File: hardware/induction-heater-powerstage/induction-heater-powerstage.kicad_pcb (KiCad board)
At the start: 2 copper layers, 112.8 x 55 mm, 17 parts, among them IC1 MAX17601ASA+, J2 Screw_Terminal_01x02, J3 Screw_Terminal_01x01, J4 Screw_Terminal_01x01, J5 Screw_Terminal_01x01, J6 Screw_Terminal_01x01, J7 RJ12, Q1 NTH4L040N120M3S, Q3 NTH4L040N120M3S

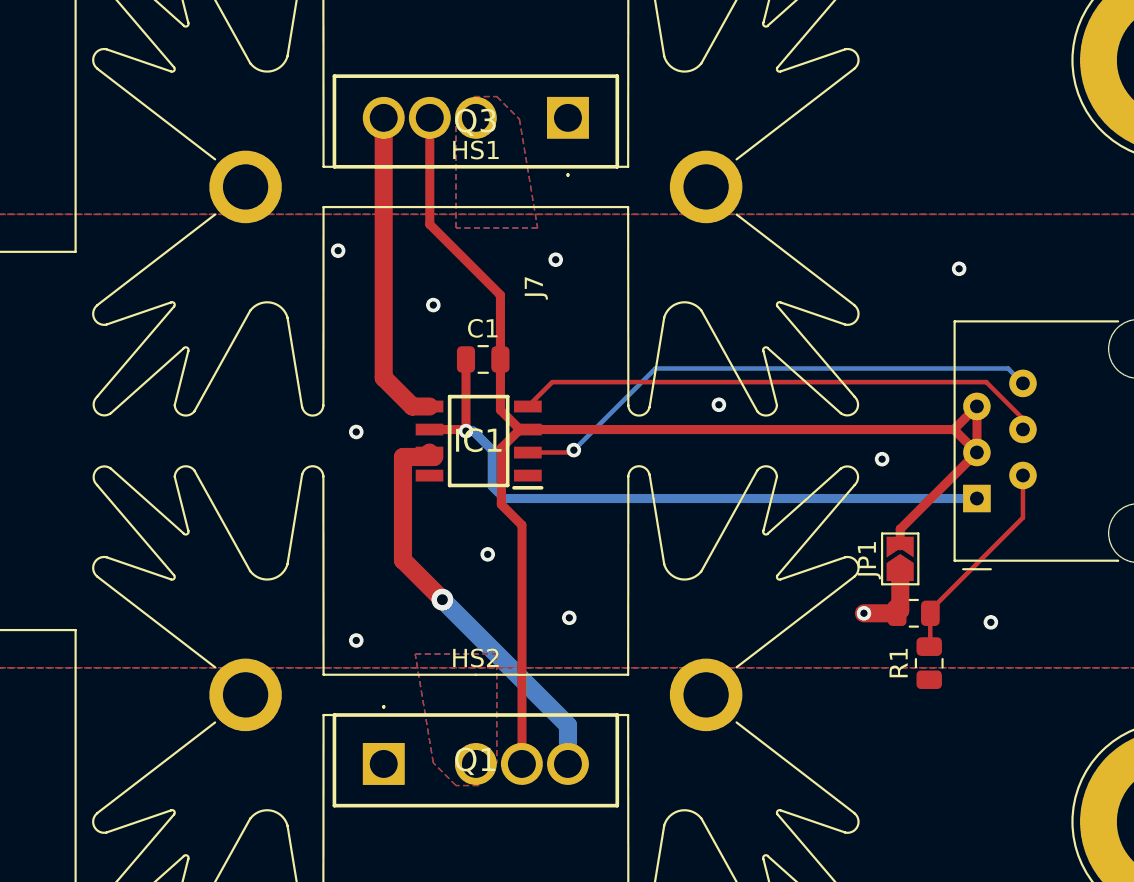
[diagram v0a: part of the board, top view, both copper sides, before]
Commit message: Fixed the mosfet driver grounds
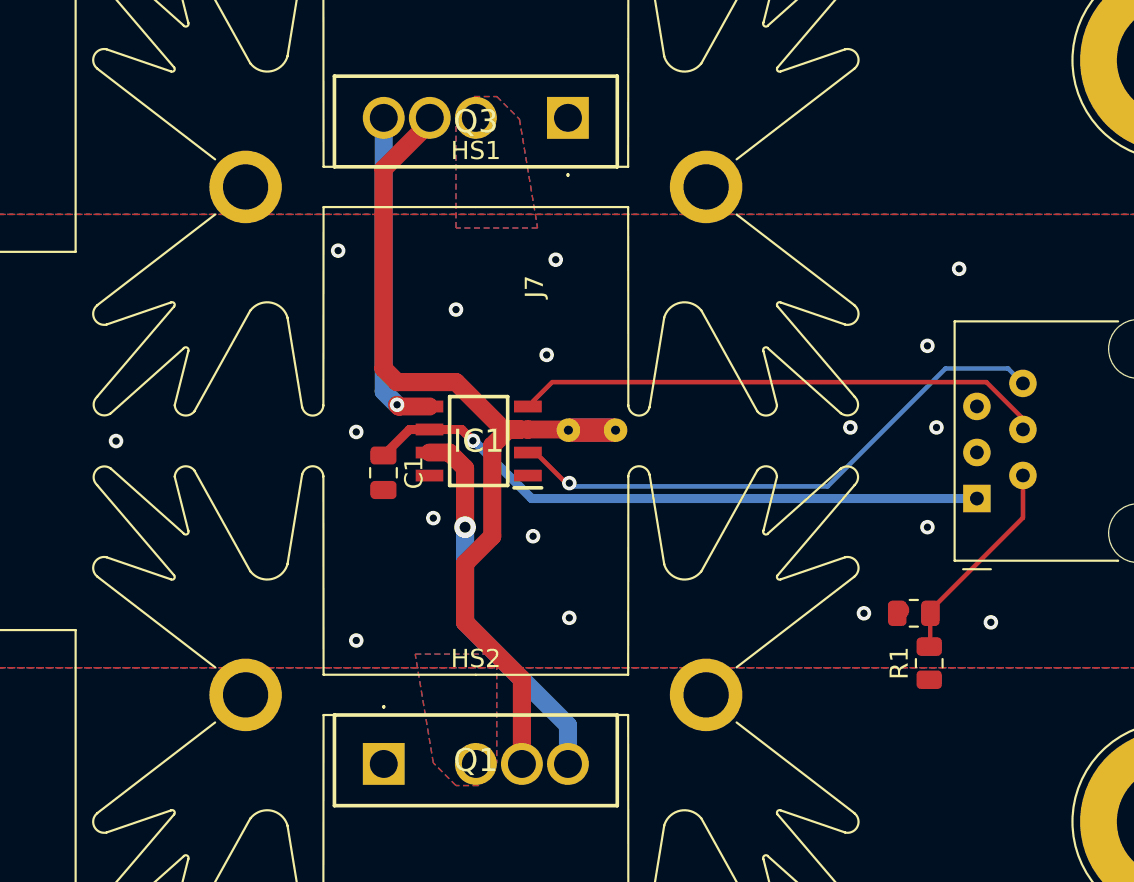
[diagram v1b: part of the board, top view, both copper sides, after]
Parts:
- removed JP1: SolderJumper_2_Open, Jumper:SolderJumper-2_P1.3mm_Open_TrianglePad1.0x1.5mm
- added NT1: NetTie_2, NetTie:NetTie-2_THT_Pad1.0mm, F.Cu at (123.2, 76.9)
- moved C1 8.33 mm to (113.0, 79.2), turned to -90 degrees
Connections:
- C1 pad 2: GND2 -> GND
- J7 pad 3: GND2 -> GND
- J7 pad 5: GND2 -> GND
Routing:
- net GND2: track 75.6 -> 47.9 mm
- net GND: track 4.18 -> 0.23 mm, vias 19 -> 24
- net Net-(IC1-VDD): track 36.9 -> 34.9 mm
- net Net-(IC1-OUTA): track 22.8 -> 21.0 mm
- net Net-(IC1-INA): track 29.6 -> 31.1 mm
- net Net-(IC1-OUTB): track 17.5 -> 18.0 mm, vias 0 -> 1

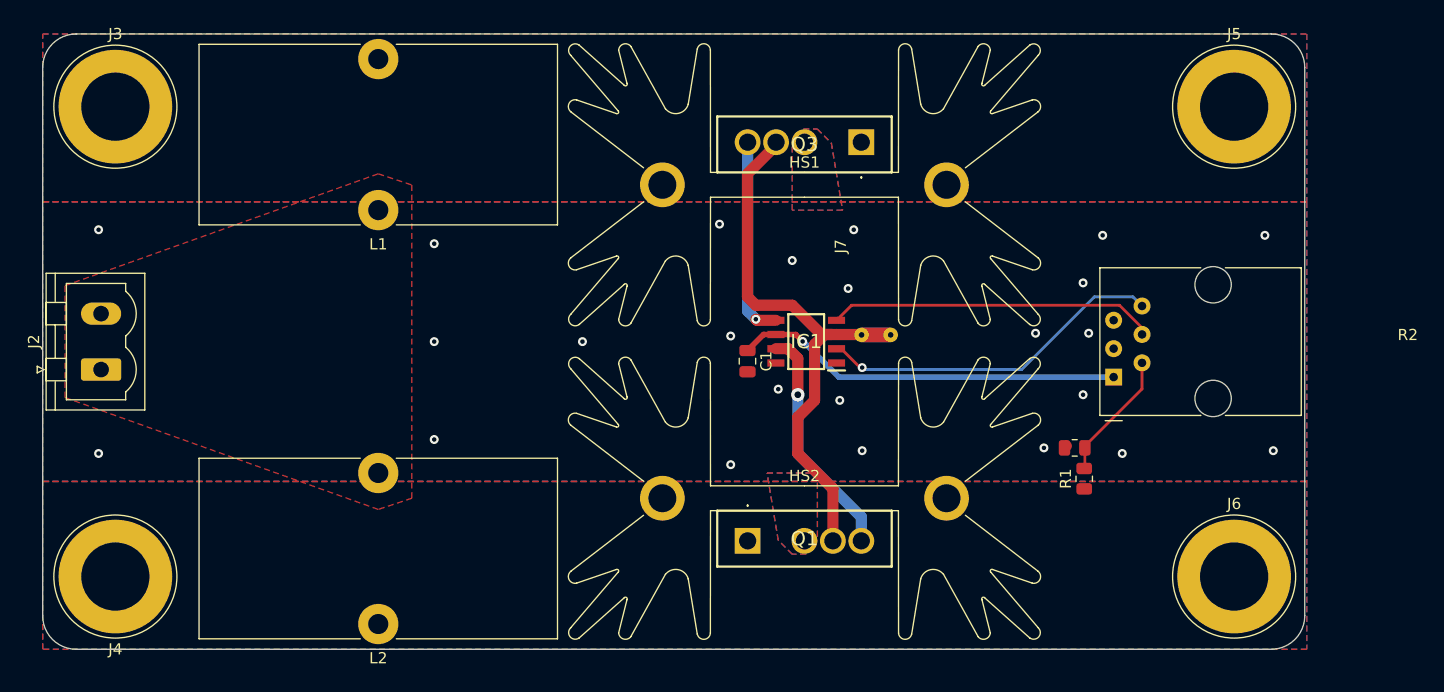
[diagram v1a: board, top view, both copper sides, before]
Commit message: Move to IGBTs
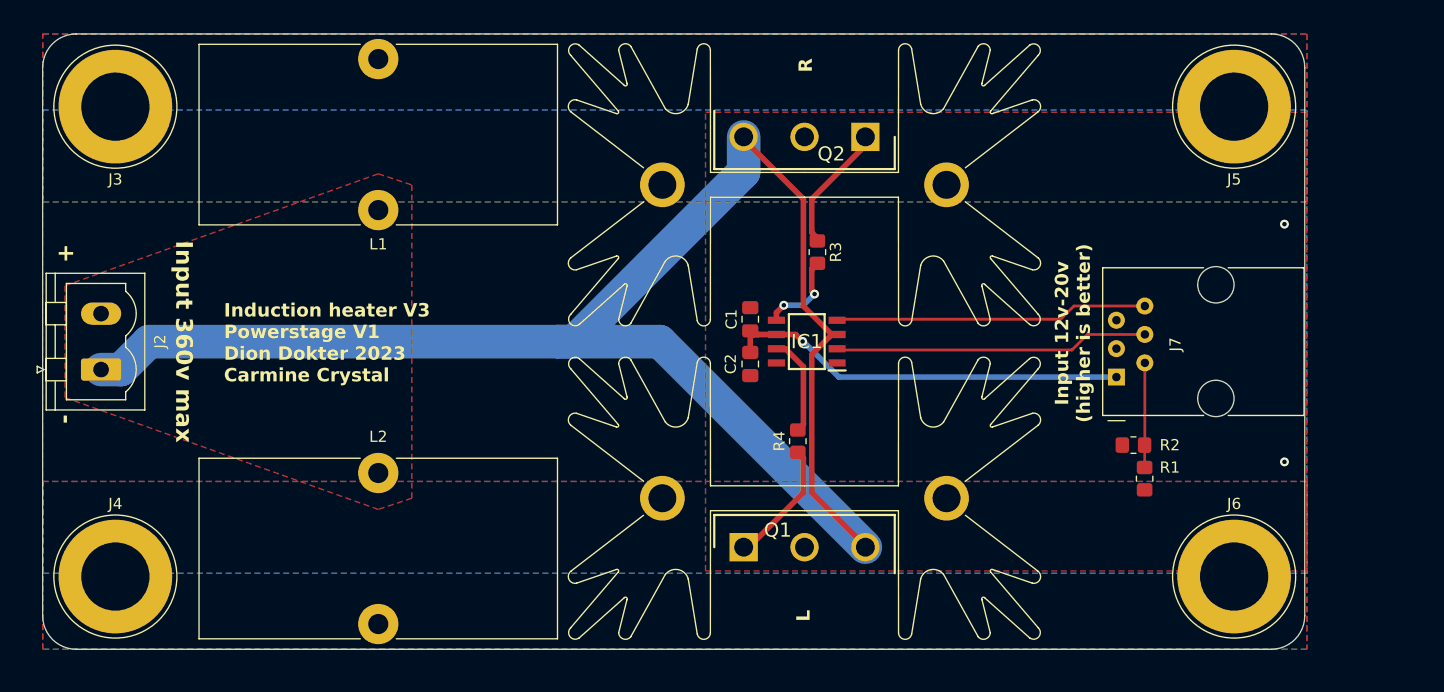
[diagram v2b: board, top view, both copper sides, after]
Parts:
- removed NT1: NetTie_2, NetTie:NetTie-2_THT_Pad1.0mm
- removed Q3: NTH4L040N120M3S, custom:NTH4L040N120M3S
- added C2: 10u, Capacitor_SMD:C_0805_2012Metric_Pad1.18x1.45mm_HandSolder, F.Cu at (113.2, 79.5)
- added Q2: IHW30N120R5XKSA1, custom:TO544P521X1592X2557-3P, F.Cu at (123.5, 59.2)
- added R3: 10, Resistor_SMD:R_0805_2012Metric_Pad1.20x1.40mm_HandSolder, F.Cu at (119.2, 69.5)
- added R4: 10, Resistor_SMD:R_0805_2012Metric_Pad1.20x1.40mm_HandSolder, F.Cu at (117.5, 86.4)
- C1: value 2.2u -> 0.1u; footprint Capacitor_SMD:C_0805_2012Metric -> Capacitor_SMD:C_0805_2012Metric_Pad1.18x1.45mm_HandSolder
- IC1: value MAX17601ASA+ -> UCC27624QDRQ1
- Q1: value NTH4L040N120M3S -> IHW30N120R5XKSA1; footprint custom:NTH4L040N120M3S -> custom:TO544P521X1592X2557-3P
- R1, R2: footprint Resistor_SMD:R_0805_2012Metric -> Resistor_SMD:R_0805_2012Metric_Pad1.20x1.40mm_HandSolder
- moved R1 5.40 mm to (148.5, 89.8)
- moved R2 5.26 mm to (147.5, 86.8)
- moved C1 3.76 mm to (113.2, 75.5), turned to 90 degrees
- moved Q1 0.67 mm to (112.7, 95.9)
- moved J7 0.25 mm to (146.0, 80.7)
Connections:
- IC1 pad 3: GND2 -> GND
- J7 pad 4: Net-(IC1-INB) -> Net-(IC1-INA)
- J7 pad 6: Net-(IC1-INA) -> Net-(IC1-INB)
- Q1 pad 1: BUS_L -> Net-(Q1-G)
- Q1 pad 2: GND -> BUS_L
- Q1 pad 3: GND2 -> GND
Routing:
- net GND: track 0.23 -> 146.2 mm, vias 24 -> 2
- net GND2: track 47.9 -> 0.00 mm
- net Net-(IC1-OUTA): track 21.0 -> 8.94 mm, vias 1 -> 0
- net Net-(Q1-G): track 0.00 -> 11.9 mm
- net Net-(Q2-G): track 0.00 -> 11.6 mm
- net Net-(IC1-OUTB): track 18.0 -> 7.84 mm, vias 1 -> 2
- net Net-(IC1-INA): track 31.1 -> 28.1 mm, vias 1 -> 0
- net Net-(J7-Pad2): track 11.8 -> 9.36 mm
- net Net-(IC1-VDD): track 34.9 -> 37.1 mm
- net Net-(IC1-INB): track 29.3 -> 28.0 mm
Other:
- board text added: "+"
- board text added: "-"
- board text added: "-> 1. VDD -> 2. Analog -> 3. GND -> 4. L -> 5. GND -> 6. R"
- board text added: "Induction heater V3 Powerstage V1 Dion Dokter 2023 Carmine Crystal"
- board text added: "Input 12v-20v (higher is better)"
- board text added: "Input 360v max"
- board text added: "L"
- board text added: "R"

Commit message: Finished board for controller
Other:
- board text added: "-> 1. VDC -> 2. Analog -> 3. GND -> 4. L -> 5. GND -> 6. R"
- board text removed: "-> 1. VDD -> 2. Analog -> 3. GND -> 4. L -> 5. GND -> 6. R"
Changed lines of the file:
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@@
   (gr_arc (start 162.815 102) (mid 161.93632 104.12132) (end 159.815 105)
     (stroke (width 0.1) (type default)) (layer "Edge.Cuts"))
-  (gr_text "-> 1. VDD\n-> 2. Analog\n-> 3. GND\n-> 4. L\n-> 5. GND\n-> 6. R" (at 153.5 77.6 180) (layer "B.SilkS")
+  (gr_text "-> 1. VDC\n-> 2. Analog\n-> 3. GND\n-> 4. L\n-> 5. GND\n-> 6. R" (at 153.5 77.6 180) (layer "B.SilkS")
     (effects (font (size 0.8 0.8) (thickness 0.2) bold) (justify left mirror))
   )
